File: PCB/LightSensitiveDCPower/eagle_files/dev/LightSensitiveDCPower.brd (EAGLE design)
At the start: 12 x 31.3 mm, 5 parts, among them SW1 PCM12SMTR

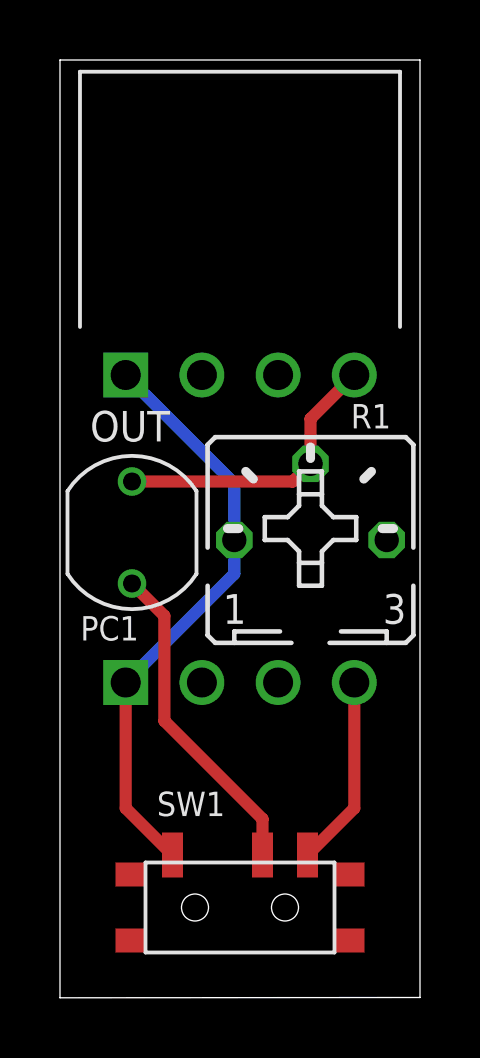
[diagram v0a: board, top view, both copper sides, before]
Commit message: Removed switch. Intended use case turned out to be out of rating.
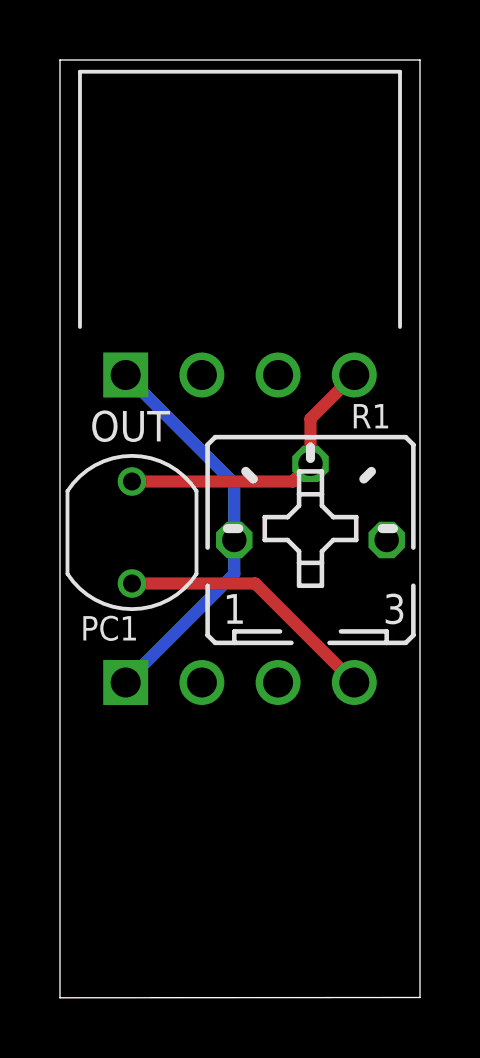
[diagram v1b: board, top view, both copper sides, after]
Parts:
- removed SW1: PCM12SMTR, freddyLibr:PCM12SMTR
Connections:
- removed net N$3: PC1.1, SW1.2
- net N$1: no longer SW1.1
- net N$2: now also PC1.1; no longer SW1.3
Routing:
- net N$3: track 10.9 -> 0.00 mm
- net N$1: track 19.6 -> 13.2 mm
- net N$2: track 6.40 -> 8.78 mm
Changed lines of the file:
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@@
 <attribute name="VALUE" x="5.2004" y="10.17" size="1.27" layer="27" ratio="10"/>
-</element>
-<element name="SW1" library="freddyLibr" package="PCM12SMTR" value="PCM12SMTR" x="6" y="3" smashed="yes">
-<attribute name="NAME" x="5.5" y="6.86" size="0.8128" layer="25" rot="R180"/>
 </element>
 <element name="IN" library="SparkFun-Connectors" package="SULLIN-1X4_HORIZ" value="" x="6" y="10.5" smashed="yes" rot="MR180">
@@
 <signals>
 <signal name="N$1">
-<contactref element="SW1" pad="1"/>
 <contactref element="R1" pad="A"/>
 <contactref element="IN" pad="P$1"/>
@@
 <wire x1="2.19" y1="10.5" x2="5.81" y2="14.12" width="0.4064" layer="16"/>
 <wire x1="5.81" y1="14.12" x2="5.81" y2="15.25" width="0.4064" layer="16"/>
-<wire x1="3.75" y1="4.75" x2="2.19" y2="6.31" width="0.4064" layer="1"/>
-<wire x1="2.19" y1="6.31" x2="2.19" y2="10.5" width="0.4064" layer="1"/>
 <wire x1="5.81" y1="15.25" x2="5.81" y2="17.13" width="0.4064" layer="16"/>
 <wire x1="5.81" y1="17.13" x2="2.19" y2="20.75" width="0.4064" layer="16"/>
 </signal>
 <signal name="N$2">
-<contactref element="SW1" pad="3"/>
 <contactref element="IN" pad="P$4"/>
-<wire x1="8.25" y1="4.75" x2="9.81" y2="6.31" width="0.4064" layer="1"/>
-<wire x1="9.81" y1="6.31" x2="9.81" y2="10.5" width="0.4064" layer="1"/>
-</signal>
-<signal name="N$3">
-<contactref element="SW1" pad="2"/>
 <contactref element="PC1" pad="1"/>
-<wire x1="6.75" y1="4.75" x2="6.75" y2="5.95" width="0.4064" layer="1"/>
-<wire x1="6.75" y1="5.95" x2="3.48" y2="9.22" width="0.4064" layer="1"/>
-<wire x1="3.48" y1="9.22" x2="3.48" y2="12.72" width="0.4064" layer="1"/>
-<wire x1="3.48" y1="12.72" x2="2.4" y2="13.8" width="0.4064" layer="1"/>
+<wire x1="2.4" y1="13.8" x2="6.51" y2="13.8" width="0.4064" layer="1"/>
+<wire x1="6.51" y1="13.8" x2="9.81" y2="10.5" width="0.4064" layer="1"/>
 </signal>
 <signal name="N$4">
